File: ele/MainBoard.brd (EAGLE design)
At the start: 134.9 x 100 mm, 120 parts, among them IC1 MCP23017SP, IC2 74HC595D, IC3 74HC595D, X1 POWER_IN, X10 M7, X2 POWER_OUT, X3 M2, X4 M4, X5 M6, X6 M8, X7 M1, X8 M3, X9 M5

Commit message: ele: Added capacitors to buttons, added description to resistor arrays.
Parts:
- added C5, C6, C7: 100n, rcl_upravena:C1206
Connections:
- net EB0: now also C5.2
- net EB1: now also C6.2
- net EB2: now also C7.2
- net GND: now also C5.1, C6.1, C7.1
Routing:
- net GND: track 12.2 -> 19.5 mm
- net EB0: track 43.9 -> 46.4 mm
- net EB2: track 43.7 -> 46.2 mm
- net EB1: track 41.5 -> 44.0 mm
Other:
- board text added: "LED1 RED EB3"
- board text added: "LED2 YELLOW EB4"
- board text added: "LED3 GREEN EB5"
- board text added: "LED4 BLUE EB6"
- board text removed: "LED1"
- board text removed: "LED2"
- board text removed: "LED3"
- board text removed: "LED4"
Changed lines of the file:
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@@
 <text x="50.803" y="34.671" size="1.5" layer="51" font="vector" ratio="20" rot="R270" align="bottom-right">-</text>
 <text x="53.721" y="36.576" size="1.5" layer="51" font="vector" ratio="20">SIG</text>
-<text x="59.326" y="1.397" size="1" layer="51" font="vector" ratio="20" align="bottom-right">SW1</text>
-<text x="62.755" y="1.397" size="1" layer="51" font="vector" ratio="20" align="bottom-right">EB0</text>
-<text x="66.946" y="1.397" size="1" layer="51" font="vector" ratio="20" align="bottom-right">SW2</text>
-<text x="77.868" y="1.397" size="1" layer="51" font="vector" ratio="20" align="bottom-right">EB2</text>
-<text x="70.375" y="1.397" size="1" layer="51" font="vector" ratio="20" align="bottom-right">EB1</text>
-<text x="74.566" y="1.397" size="1" layer="51" font="vector" ratio="20" align="bottom-right">SW3</text>
-<text x="98.789" y="6.223" size="1" layer="51" font="vector" ratio="20" rot="R180" align="bottom-right">LED1</text>
-<text x="92.439" y="6.223" size="1" layer="51" font="vector" ratio="20" rot="R180" align="bottom-right">LED2</text>
-<text x="86.978" y="6.223" size="1" layer="51" font="vector" ratio="20" rot="R180" align="bottom-right">LED3</text>
-<text x="81.009" y="6.223" size="1" layer="51" font="vector" ratio="20" rot="R180" align="bottom-right">LED4</text>
-<text x="81.009" y="4.318" size="1" layer="51" font="vector" ratio="20" rot="R180" align="bottom-right">EB6</text>
-<text x="86.978" y="4.318" size="1" layer="51" font="vector" ratio="20" rot="R180" align="bottom-right">EB5</text>
-<text x="92.439" y="4.318" size="1" layer="51" font="vector" ratio="20" rot="R180" align="bottom-right">EB4</text>
-<text x="98.789" y="4.318" size="1" layer="51" font="vector" ratio="20" rot="R180" align="bottom-right">EB3</text>
+<text x="63.517" y="1.905" size="1" layer="51" font="vector" ratio="20" align="bottom-right">SW1</text>
+<text x="59.326" y="1.905" size="1" layer="51" font="vector" ratio="20" align="bottom-right">EB0</text>
+<text x="71.01" y="1.905" size="1" layer="51" font="vector" ratio="20" align="bottom-right">SW2</text>
+<text x="74.693" y="1.905" size="1" layer="51" font="vector" ratio="20" align="bottom-right">EB2</text>
+<text x="67.073" y="1.905" size="1" layer="51" font="vector" ratio="20" align="bottom-right">EB1</text>
+<text x="78.757" y="1.905" size="1" layer="51" font="vector" ratio="20" align="bottom-right">SW3</text>
+<text x="99.678" y="6.223" size="1" layer="51" font="vector" ratio="20" rot="R180" align="bottom-center">LED1
+RED
+EB3</text>
+<text x="93.963" y="6.223" size="1" layer="51" font="vector" ratio="20" rot="R180" align="bottom-center">LED2
+YELLOW
+EB4</text>
+<text x="88.248" y="6.223" size="1" layer="51" font="vector" ratio="20" rot="R180" align="bottom-center">LED3
+GREEN
+EB5</text>
+<text x="82.279" y="6.223" size="1" layer="51" font="vector" ratio="20" rot="R180" align="bottom-center">LED4
+BLUE
+EB6</text>
 <text x="83.944" y="18.288" size="1.5" layer="51" font="vector" ratio="20" rot="R90">SCL</text>
 <text x="85.849" y="18.288" size="1.5" layer="51" font="vector" ratio="20" rot="R90">SDA</text>
@@
 <attribute name="MF" value="" x="77.47" y="30.48" size="1.778" layer="27" rot="R90" display="off"/>
 <attribute name="MPN" value="" x="77.47" y="30.48" size="1.778" layer="27" rot="R90" display="off"/>
+<attribute name="NAME" x="80.01" y="44.45" size="1.016" layer="25" font="vector" ratio="20" rot="R90"/>
 <attribute name="OC_FARNELL" value="unknown" x="77.47" y="30.48" size="1.778" layer="27" rot="R90" display="off"/>
 <attribute name="OC_MOUSER" value="652-4614X-2LF-180" x="77.47" y="30.48" size="1.778" layer="27" rot="R90" display="off"/>
@@
 <attribute name="MF" value="" x="62.23" y="30.48" size="1.778" layer="27" rot="R270" display="off"/>
 <attribute name="MPN" value="" x="62.23" y="30.48" size="1.778" layer="27" rot="R270" display="off"/>
+<attribute name="NAME" x="63.5" y="46.99" size="1.016" layer="25" font="vector" ratio="20" rot="R270"/>
 <attribute name="OC_FARNELL" value="unknown" x="62.23" y="30.48" size="1.778" layer="27" rot="R270" display="off"/>
 <attribute name="OC_MOUSER" value="652-4614X-2LF-180" x="62.23" y="30.48" size="1.778" layer="27" rot="R270" display="off"/>
@@
 <attribute name="MF" value="" x="66.04" y="68.58" size="1.778" layer="27" rot="R270" display="off"/>
 <attribute name="MPN" value="" x="66.04" y="68.58" size="1.778" layer="27" rot="R270" display="off"/>
+<attribute name="NAME" x="67.31" y="86.36" size="1.016" layer="25" font="vector" ratio="20" rot="R270"/>
 <attribute name="OC_FARNELL" value="unknown" x="66.04" y="68.58" size="1.778" layer="27" rot="R270" display="off"/>
 <attribute name="OC_MOUSER" value="652-4614X-2LF-180" x="66.04" y="68.58" size="1.778" layer="27" rot="R270" display="off"/>
@@
 <attribute name="MF" value="" x="99.06" y="81.28" size="1.778" layer="27" rot="R270" display="off"/>
 <attribute name="MPN" value="" x="99.06" y="81.28" size="1.778" layer="27" rot="R270" display="off"/>
+<attribute name="NAME" x="100.33" y="99.06" size="1.016" layer="25" font="vector" ratio="20" rot="R270"/>
 <attribute name="OC_FARNELL" value="unknown" x="99.06" y="81.28" size="1.778" layer="27" rot="R270" display="off"/>
 <attribute name="OC_MOUSER" value="652-4614X-2LF-180" x="99.06" y="81.28" size="1.778" layer="27" rot="R270" display="off"/>
@@
 <attribute name="MF" value="" x="62.23" y="68.58" size="1.778" layer="27" rot="R270" display="off"/>
 <attribute name="MPN" value="" x="62.23" y="68.58" size="1.778" layer="27" rot="R270" display="off"/>
+<attribute name="NAME" x="63.5" y="86.36" size="1.016" layer="25" font="vector" ratio="20" rot="R270"/>
 <attribute name="OC_FARNELL" value="unknown" x="62.23" y="68.58" size="1.778" layer="27" rot="R270" display="off"/>
 <attribute name="OC_MOUSER" value="652-4614X-2LF-180" x="62.23" y="68.58" size="1.778" layer="27" rot="R270" display="off"/>
@@
 <attribute name="VALUE" x="14.9606" y="9.6774" size="1.27" layer="27" ratio="10" rot="R180"/>
 </element>
+<element name="C5" library="rcl_upravena" package="C1206" value="100n" x="60.198" y="2.286" rot="MR180"/>
+<element name="C6" library="rcl_upravena" package="C1206" value="100n" x="67.945" y="2.286" rot="MR0"/>
+<element name="C7" library="rcl_upravena" package="C1206" value="100n" x="75.565" y="2.286" rot="MR0"/>
 </elements>
 <signals>
@@
 <via x="55.626" y="79.121" extent="1-16" drill="0.35"/>
 <contactref element="R19" pad="1"/>
+<contactref element="C5" pad="1"/>
+<contactref element="C6" pad="1"/>
+<contactref element="C7" pad="1"/>
+<wire x1="58.798" y1="2.286" x2="58.0644" y2="3.0196" width="0.4064" layer="16"/>
+<wire x1="58.0644" y1="3.0196" x2="58.0644" y2="4.3688" width="0.4064" layer="16"/>
+<wire x1="69.345" y1="2.286" x2="70.2056" y2="3.1466" width="0.4064" layer="16"/>
+<wire x1="70.2056" y1="3.1466" x2="70.2056" y2="4.3688" width="0.4064" layer="16"/>
+<wire x1="76.965" y1="2.286" x2="77.8256" y2="3.1466" width="0.4064" layer="16"/>
+<wire x1="77.8256" y1="3.1466" x2="77.8256" y2="4.3688" width="0.4064" layer="16"/>
 </signal>
 <signal name="TXD0">
@@
 <wire x1="56.515" y1="34.925" x2="58.460890625" y2="34.925" width="0.2" layer="16"/>
 <wire x1="58.460890625" y1="34.925" x2="60.338465625" y2="33.047425" width="0.2" layer="16"/>
+<contactref element="C5" pad="2"/>
+<wire x1="61.598" y1="2.286" x2="62.5856" y2="3.2736" width="0.4064" layer="16"/>
+<wire x1="62.5856" y1="3.2736" x2="62.5856" y2="4.3688" width="0.4064" layer="16"/>
 <wire x1="62.5856" y1="4.3688" x2="62.5856" y2="10.8712" width="0" layer="19" extent="1-1"/>
 </signal>
@@
 <wire x1="56.515" y1="32.385" x2="58.712059375" y2="32.385" width="0.2" layer="16"/>
 <wire x1="58.712059375" y1="32.385" x2="60.617059375" y2="30.48" width="0.2" layer="16"/>
+<contactref element="C6" pad="2"/>
+<wire x1="66.545" y1="2.286" x2="65.6844" y2="3.1466" width="0.4064" layer="16"/>
+<wire x1="65.6844" y1="3.1466" x2="65.6844" y2="4.3688" width="0.4064" layer="16"/>
 <wire x1="65.6844" y1="4.3688" x2="65.6844" y2="10.8712" width="0" layer="19" extent="1-1"/>
 </signal>
@@
 <wire x1="56.515" y1="29.845" x2="58.58126875" y2="29.845" width="0.2" layer="16"/>
 <wire x1="58.58126875" y1="29.845" x2="60.27411875" y2="28.15215" width="0.2" layer="16"/>
+<contactref element="C7" pad="2"/>
+<wire x1="74.165" y1="2.286" x2="73.3044" y2="3.1466" width="0.4064" layer="16"/>
+<wire x1="73.3044" y1="3.1466" x2="73.3044" y2="4.3688" width="0.4064" layer="16"/>
 <wire x1="73.3044" y1="10.8712" x2="73.3044" y2="4.3688" width="0" layer="19" extent="1-1"/>
 </signal>

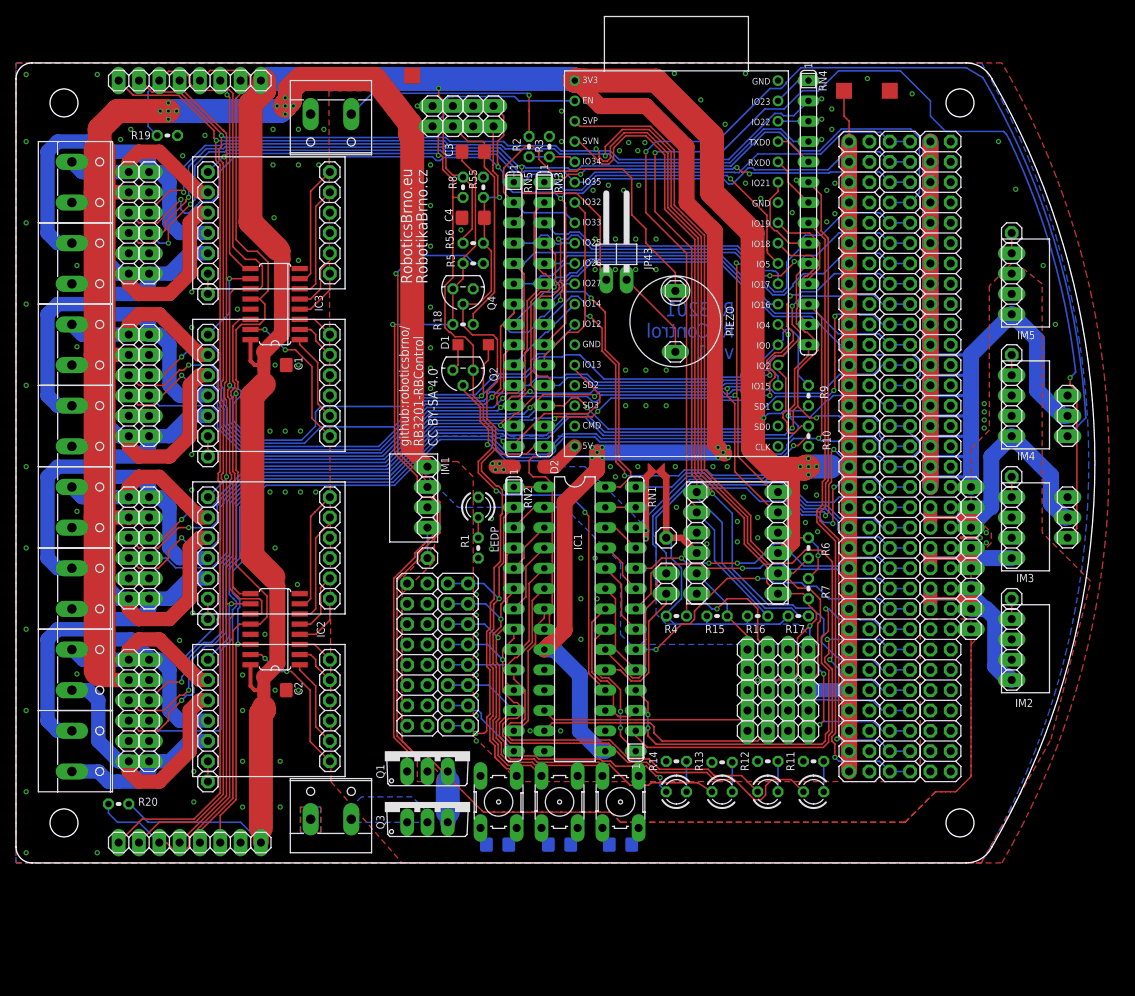
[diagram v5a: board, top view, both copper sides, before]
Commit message: ele: MainBoard - fix bug with stepdowns - reroute all routes from stepdowns (please check @cednik)
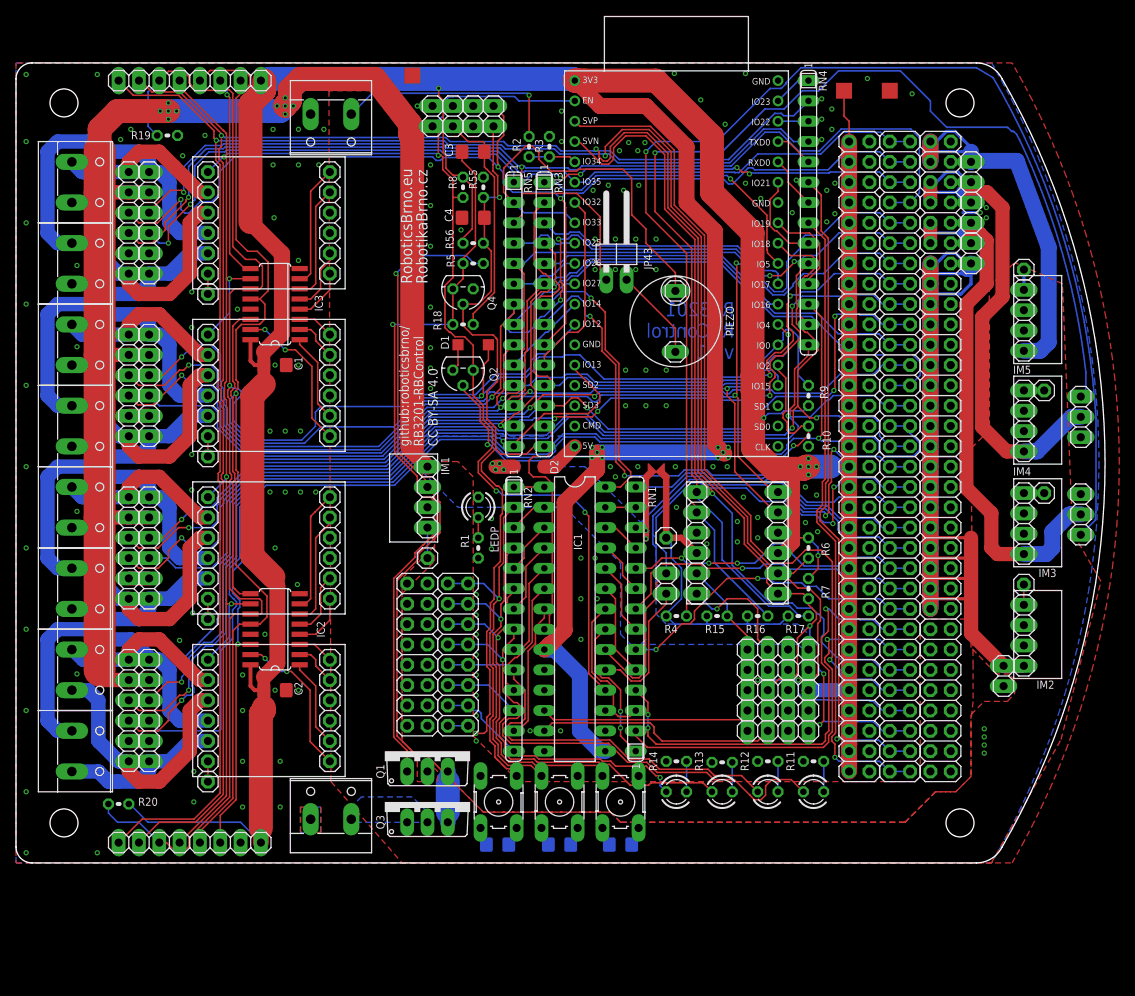
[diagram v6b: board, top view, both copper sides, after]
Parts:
- moved JP10 40.6 mm to (119.4, 86.4)
- moved JP12 40.6 mm to (115.6, 71.1)
- moved JP13 40.6 mm to (115.6, 30.5)
- moved JP8 40.6 mm to (119.4, 76.2)
- moved JP9 40.6 mm to (119.4, 81.3)
- moved JP7 8.19 mm to (123.4, 23.4)
- moved JP4 6.02 mm to (128.5, 59.1)
- moved IM5 4.82 mm to (124.7, 62.7)
- moved JP5 4.82 mm to (126.0, 74.2)
- moved JP3 4.54 mm to (128.5, 46.2)
- moved IM4 2.44 mm to (124.7, 50.2)
- moved IM2 2.34 mm to (124.7, 23.4)
- moved JP2 2.34 mm to (126.0, 34.8)
- moved JP23 1.69 mm to (133.1, 43.6)
- moved JP22 1.66 mm to (133.1, 55.8), turned to 270 degrees
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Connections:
- net N$2 renamed STEP2_EN
- net N$5 renamed STEP3_EN
- net N$7 renamed STEP4_EN
- net N$8 renamed STEP5_EN
- net +5V: now also JP13.10, JP13.12, JP13.14, JP13.16, JP13.2, JP13.4, JP13.6, JP13.8; no longer JP12.10, JP12.12, JP12.14, JP12.16, JP12.2, JP12.4, JP12.6, JP12.8
- net 5V_2: now also JP12.10, JP12.12, JP12.14, JP12.16, JP12.2, JP12.4, JP12.6, JP12.8, JP13.18, JP13.20, JP13.22, JP13.24, JP13.26, JP13.28, JP13.30, JP13.32
- net 5V_3: now also JP23.2
- net 5V_4: now also JP22.2; no longer JP23.2
- net 5V_5: no longer JP13.10, JP13.12, JP13.14, JP13.16, JP13.18, JP13.2, JP13.20, JP13.22, JP13.24, JP13.26, JP13.28, JP13.30, JP13.32, JP13.4, JP13.6, JP13.8, JP22.2
- net A5V: now also JP23.1; no longer JP22.1
- net B5V: now also JP22.1; no longer JP23.1
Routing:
- net 5V_5: track 162.8 -> 51.1 mm
- net 5V_2: track 42.7 -> 153.9 mm
- net 5V_3: track 31.1 -> 71.9 mm
- net B5V: track 174.6 -> 156.1 mm, vias 2 -> 1
- net 5V_4: track 54.1 -> 71.3 mm
- net A5V: track 160.6 -> 172.3 mm
- net GND: track 19.5 -> 17.2 mm, vias 155 -> 151
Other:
- board size 134.9 x 100 mm -> 136.1 x 100 mm
- board text added: "IM1+IM2"
- board text added: "SW1 EB0"
- board text added: "SW2 EB1"
- board text added: "SW3 EB2"
- board text removed: "SW1"
- board text removed: "SW2"
- board text removed: "SW3"

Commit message: ele: Tune layout, improve GND coherence
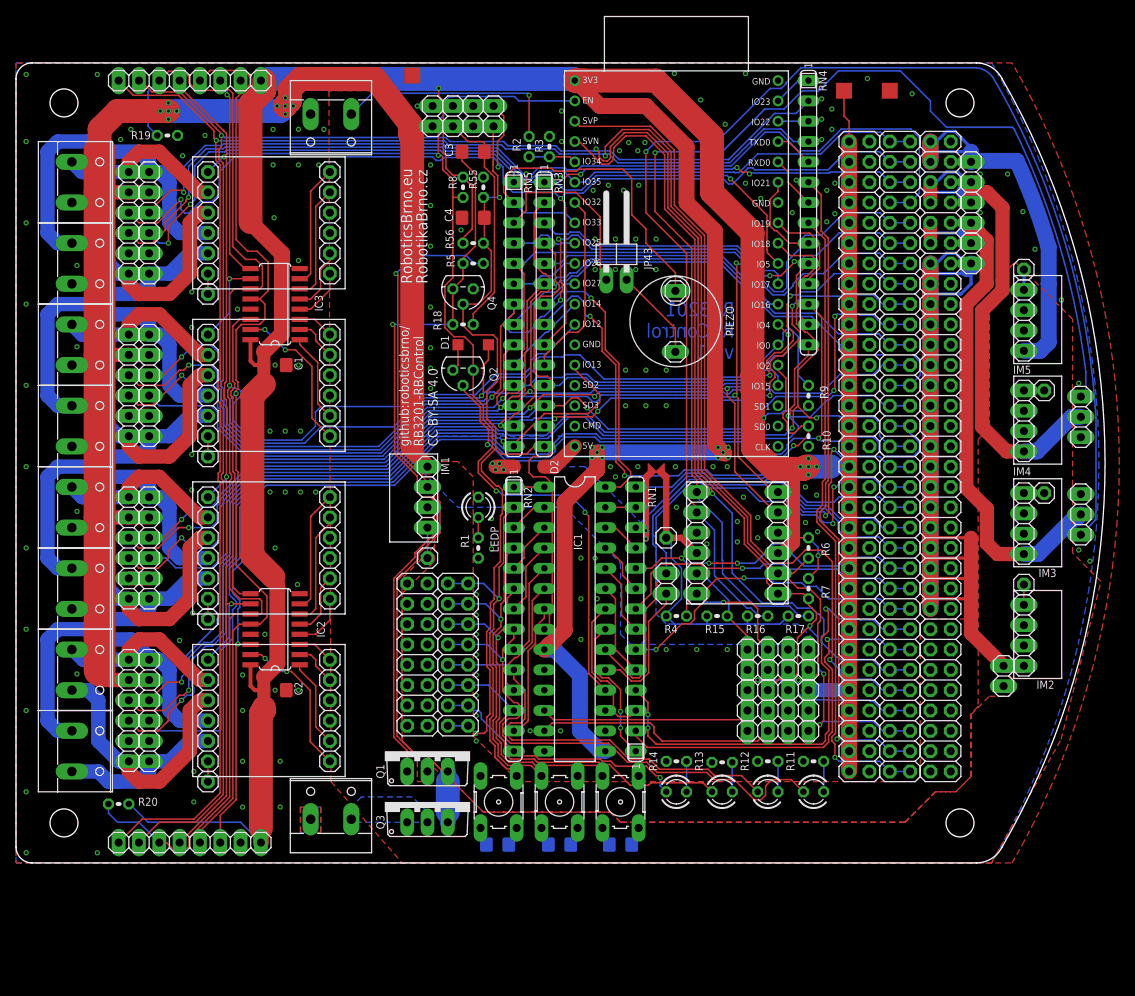
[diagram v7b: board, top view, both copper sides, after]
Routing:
- net ENC7B_: track 49.4 -> 45.8 mm
- net GND: track 17.2 -> 14.9 mm, vias 151 -> 156
- net 5V_3: track 71.9 -> 70.7 mm
- net SDA5V: track 20.9 -> 19.9 mm
- net A5V: track 172.3 -> 173.3 mm
- net B5V: track 156.1 -> 157.0 mm
- net ENC8A: track 140.5 -> 141.4 mm
- net EA2: track 41.9 -> 42.7 mm
- net ENC7A: track 145.7 -> 145.0 mm
- net ENC8B: track 111.3 -> 112.1 mm
- net IO39: track 100.2 -> 100.8 mm
- net SCL5V: track 14.9 -> 15.5 mm
